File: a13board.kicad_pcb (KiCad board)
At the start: 4 copper layers, 50 x 90.4 mm, 152 parts, among them P1 CONN_20, P2 CONN_20, P3 CONN_20, P4 CONN_20, P5 CONN_20, U1 H27UBG8T2A/TSOP48, U2 A13, U3 H5TQ2G43CFR, U4 H5TQ2G43CFR, U5 OLIMEX_IC_AXP209, U6 SY8008BAAC, U7 SY8008BAAC, X1 CRYSTAL4

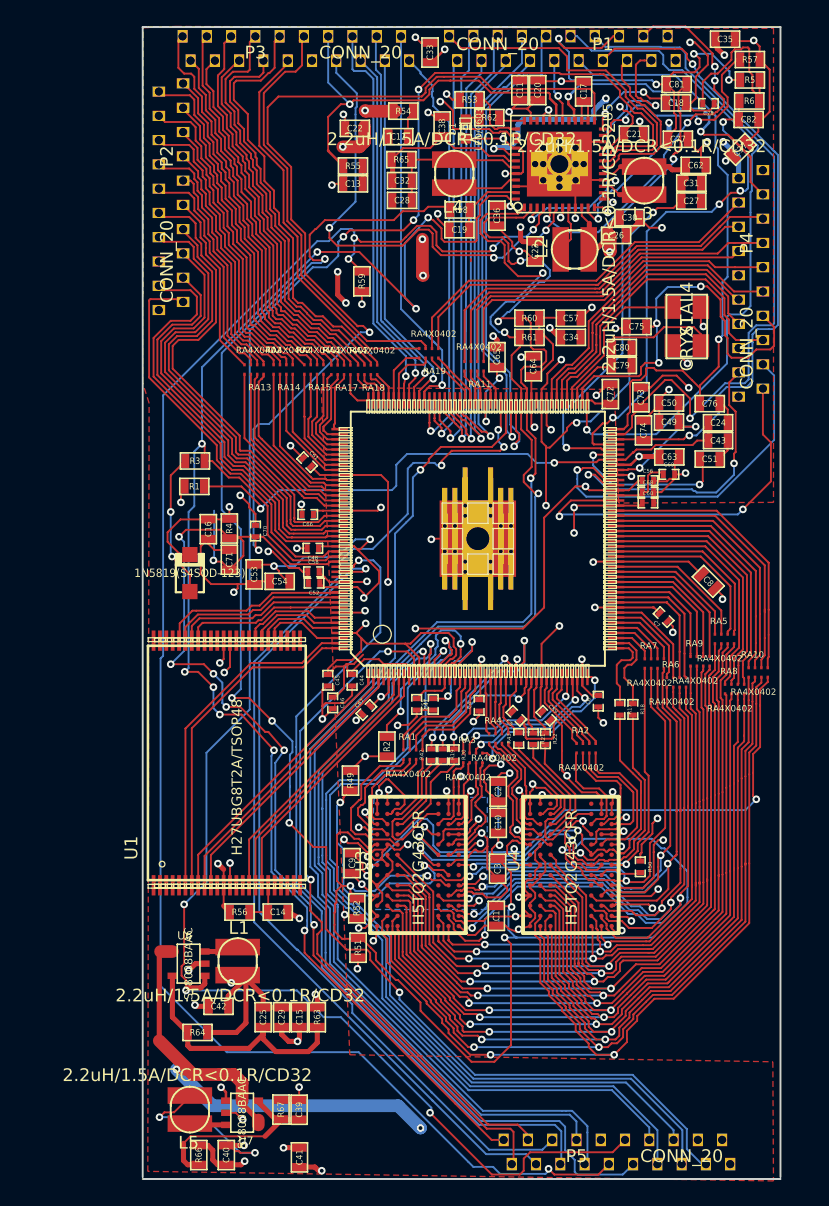
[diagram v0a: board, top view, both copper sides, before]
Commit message: Updated layout with people's suggestions
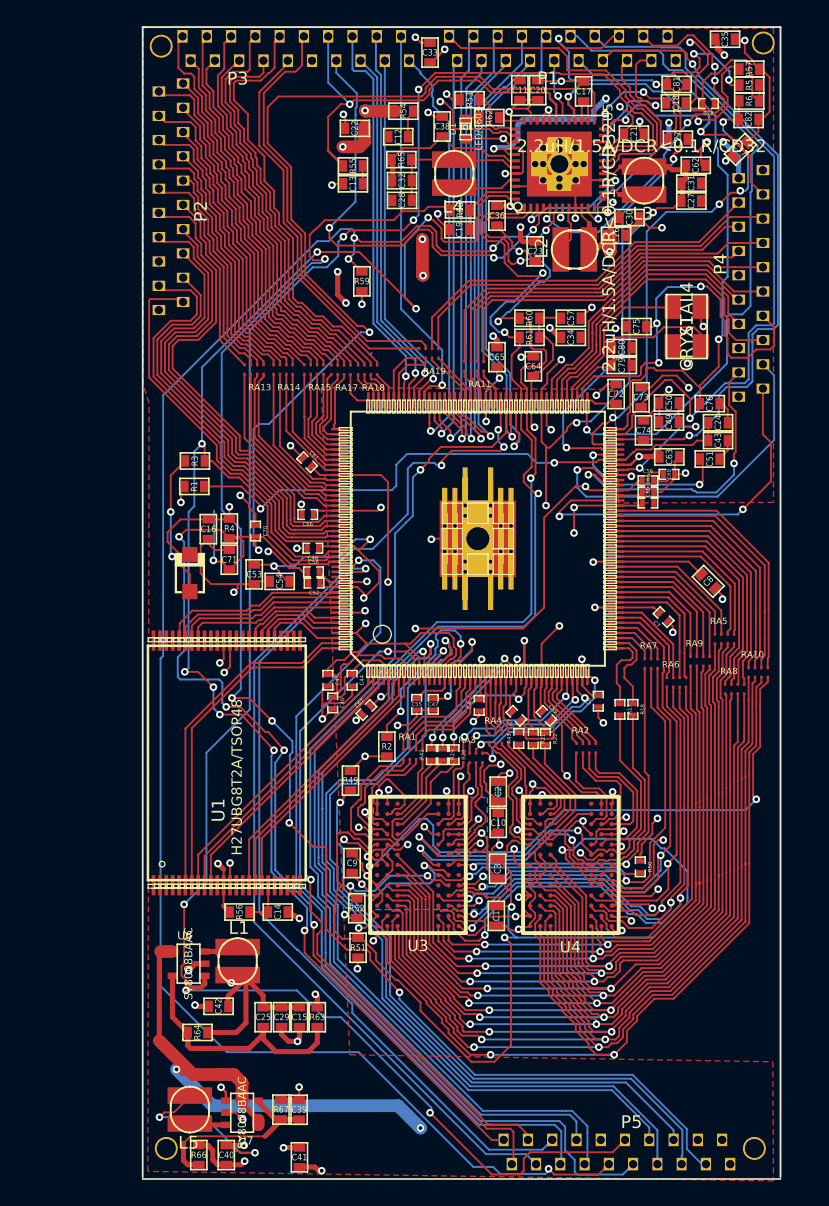
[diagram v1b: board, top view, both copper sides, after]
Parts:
- added P6: CONN_1, 1pin, F.Cu at (89.0, 138.8)
- added P7: CONN_1, 1pin, F.Cu at (135.9, 52.1)
- added P8: CONN_1, 1pin, F.Cu at (88.7, 52.4)
- added P9: CONN_1, 1pin, F.Cu at (135.2, 138.8)
- C10, C11, C12, C13, C14, C15, C16, C17, C18, C19, C20, C21, C22, C23, C24, C25, C26, C27, C28, C29, C30, C31, C32, C33, C34, C35, C36, C37, C38, C39, C40, C41, C42, C43, C49, C50, C51, C53, C54, C57, C62, C63, C64, C65, C71, C72, C73, C74, C75, C76, C77, C79, C8, C80, C81, C82, C9: footprint SM0603_Capa -> SM0603A
- R1, R2, R3, R4, R49, R5, R51, R52, R53, R54, R55, R56, R57, R58, R59, R6, R60, R61, R62, R63, R64, R65, R66, R67: footprint SM0603 -> SM0603A
- moved R57 0.75 mm to (134.8, 54.1)
- moved C72 0.45 mm to (124.3, 79.7)
- moved R5 0.40 mm to (134.8, 55.4)
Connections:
- U5 pad GND: GND -> (no net)
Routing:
- net +3.3V: track 184.0 -> 175.6 mm
- net /power/VDD_CPU: track 129.2 -> 133.8 mm
- net VPP: track 149.1 -> 147.0 mm
- net IPSOUT: track 229.5 -> 231.3 mm
- net N-00000277: track 12.8 -> 11.4 mm
- net RESET: track 162.5 -> 162.3 mm, vias 9 -> 7

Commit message: Used polygon for power pins
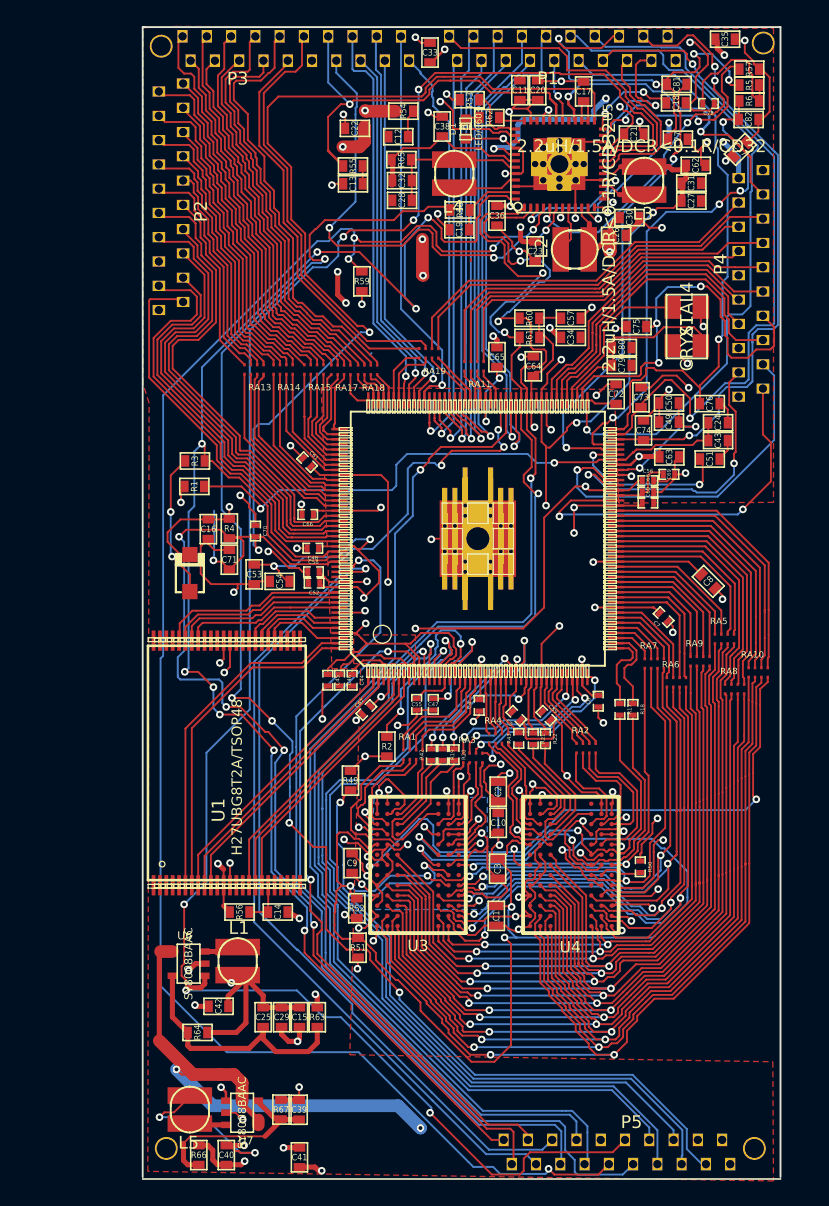
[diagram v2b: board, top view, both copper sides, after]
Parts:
- moved C46 1.87 mm to (102.7, 102.1)
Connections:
- U5 pad GND: (no net) -> GND
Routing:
- net /power/VDD_CPU: track 133.8 -> 126.1 mm
- net GND: track 265.1 -> 260.5 mm
- added copper zone on F.Cu, net /power/VDD_CPU

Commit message: Fixed some power issues
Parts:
- moved C40 9.03 mm to (102.0, 135.8)
- moved R66 8.53 mm to (99.3, 135.8)
- moved R63 8.15 mm to (92.8, 128.6)
- moved C41 5.45 mm to (103.5, 135.8)
- moved R64 2.68 mm to (93.9, 128.6), turned to 90 degrees
- moved C42 2.27 mm to (95.2, 128.6), turned to 90 degrees
- moved C39 1.18 mm to (100.7, 135.8)
- moved L5 0.18 mm to (90.8, 135.7)
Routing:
- net N-00000172: track 15.1 -> 5.19 mm
- net IPSOUT: track 231.3 -> 224.1 mm, vias 13 -> 14
- net N-00000171: track 20.2 -> 16.7 mm
- net +3.3V: track 175.6 -> 172.2 mm
- net VMEM: track 170.3 -> 172.9 mm, vias 30 -> 26
- net GND: track 260.5 -> 259.7 mm, vias 76 -> 74

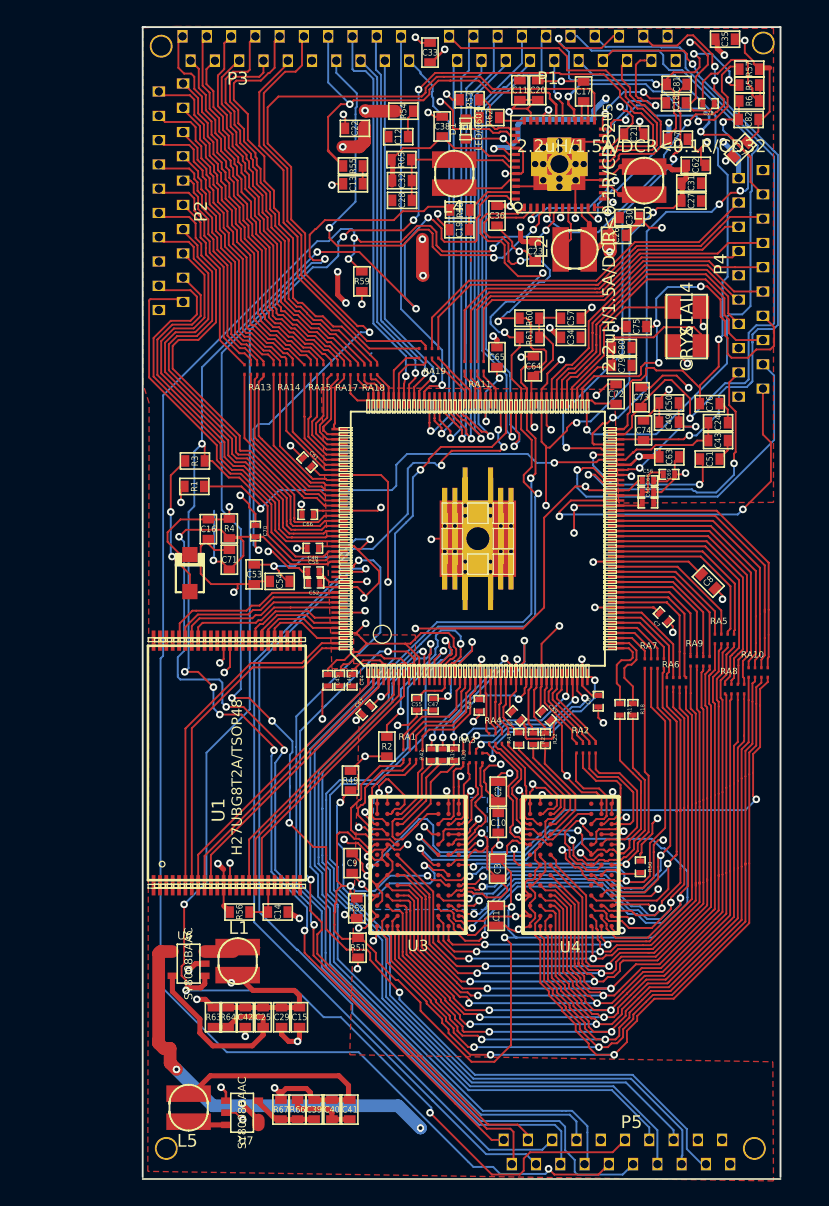
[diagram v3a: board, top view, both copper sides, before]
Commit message: A little fit of border clearance fixed
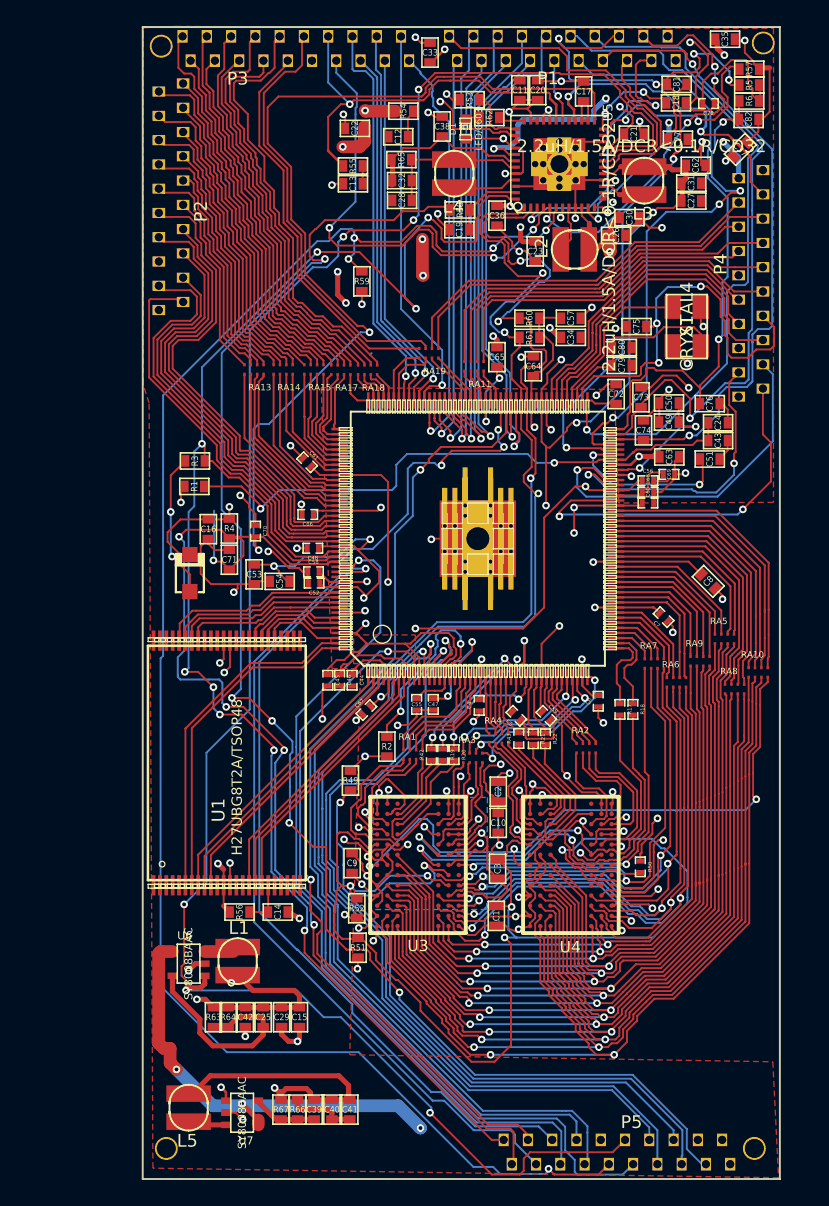
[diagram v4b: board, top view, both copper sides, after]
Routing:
- net TPX2: track 53.9 -> 52.5 mm
- net TPY2: track 49.1 -> 49.9 mm
- net LRADC: track 51.1 -> 50.4 mm
- net N-00000278: track 38.9 -> 39.6 mm
- net PB17: track 64.6 -> 64.0 mm
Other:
- outline, holes or cut-outs redrawn

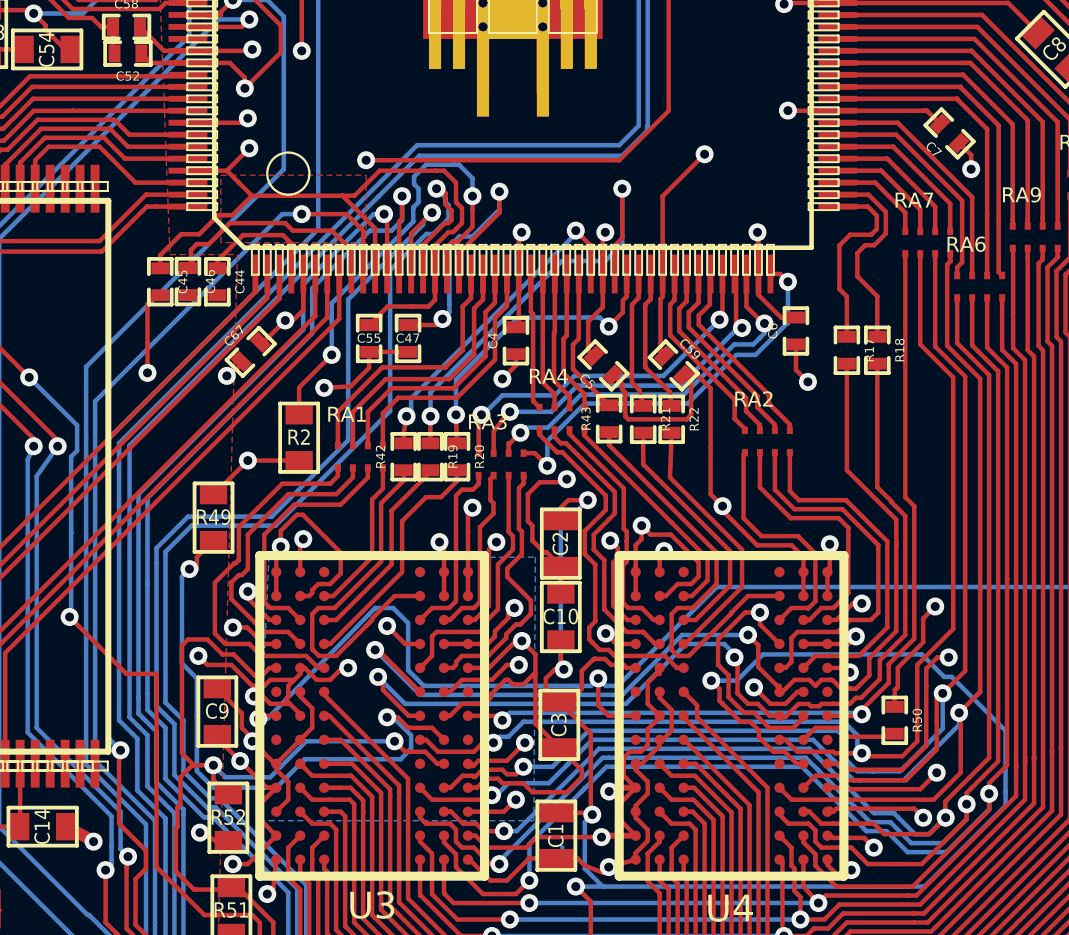
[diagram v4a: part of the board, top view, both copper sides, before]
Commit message: Improved data lines
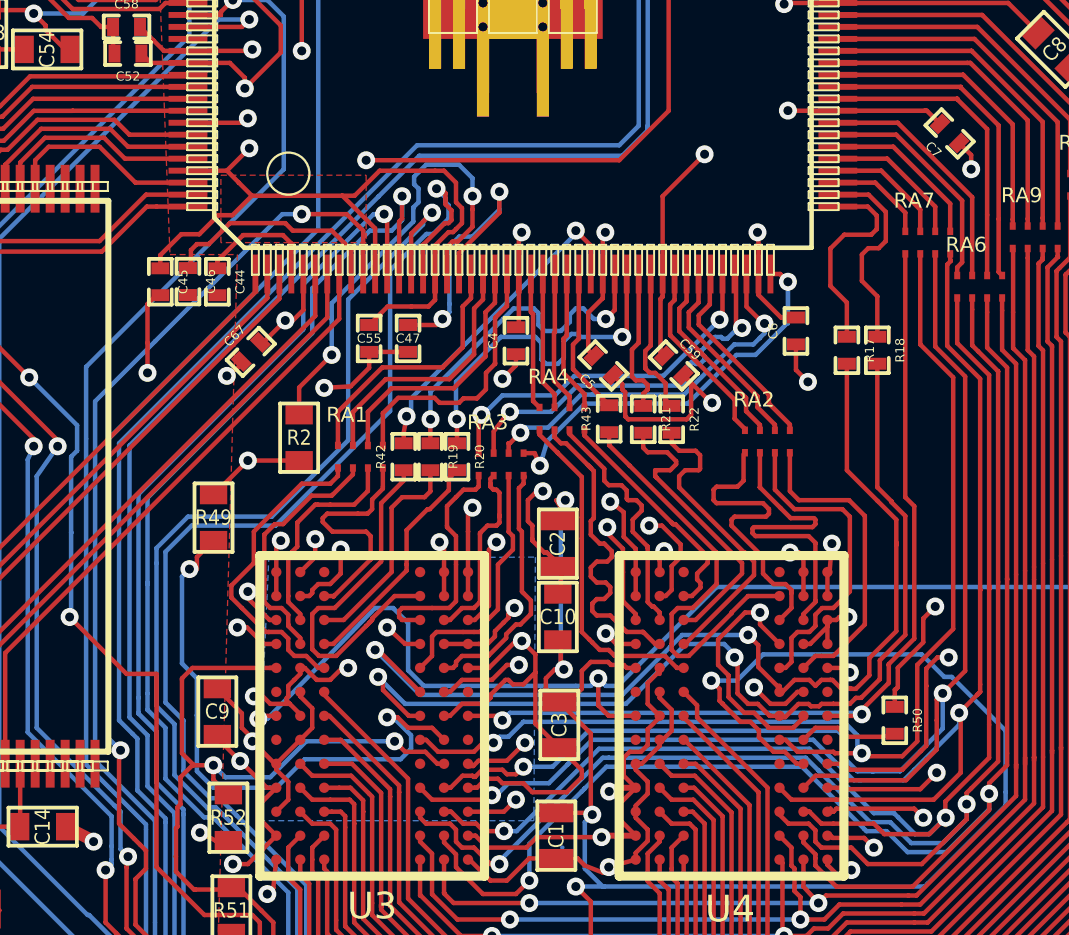
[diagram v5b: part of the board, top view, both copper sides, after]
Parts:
- moved C10 0.10 mm to (115.0, 113.3)
- moved C2 0.10 mm to (115.0, 110.8)
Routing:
- net GND: track 259.3 -> 248.0 mm, vias 74 -> 76
- net /DRAM/CPU_DQS0: track 15.1 -> 11.7 mm
- net /DRAM/DDR3_D0: track 5.26 -> 8.15 mm
- net N-0000056: track 106.4 -> 104.1 mm
- net /DRAM/DDR3_D12: track 8.11 -> 10.4 mm
- net /DRAM/DDR3_D8: track 8.72 -> 10.9 mm
- net /DRAM/DDR3_D1: track 6.19 -> 8.02 mm
- net /DRAM/DDR3_D4: track 12.3 -> 10.7 mm
- net /DRAM/CPU_DQS0_N: track 10.2 -> 11.9 mm
- net /DRAM/DDR3_D9: track 9.74 -> 11.4 mm
- net /DRAM/DDR3_D6: track 9.97 -> 8.37 mm
- net /DRAM/DDR3_DQS1: track 8.33 -> 9.91 mm
- net /DRAM/DDR3_D14: track 12.2 -> 10.7 mm
- net /DRAM/DDR3_DQS1_N: track 8.88 -> 10.4 mm
- net /DRAM/DDR3_D10: track 11.5 -> 10.4 mm
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
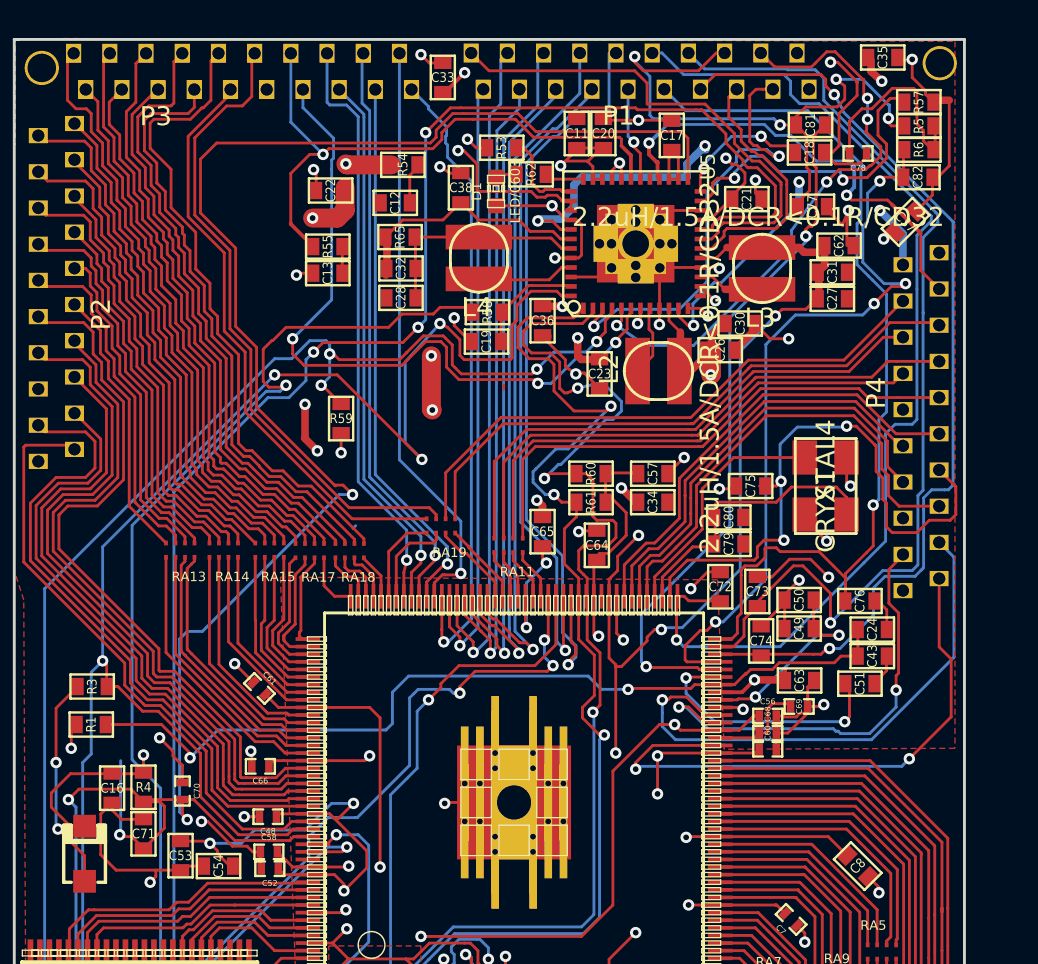
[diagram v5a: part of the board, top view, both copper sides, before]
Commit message: Fixed some symbols, hidden some silk
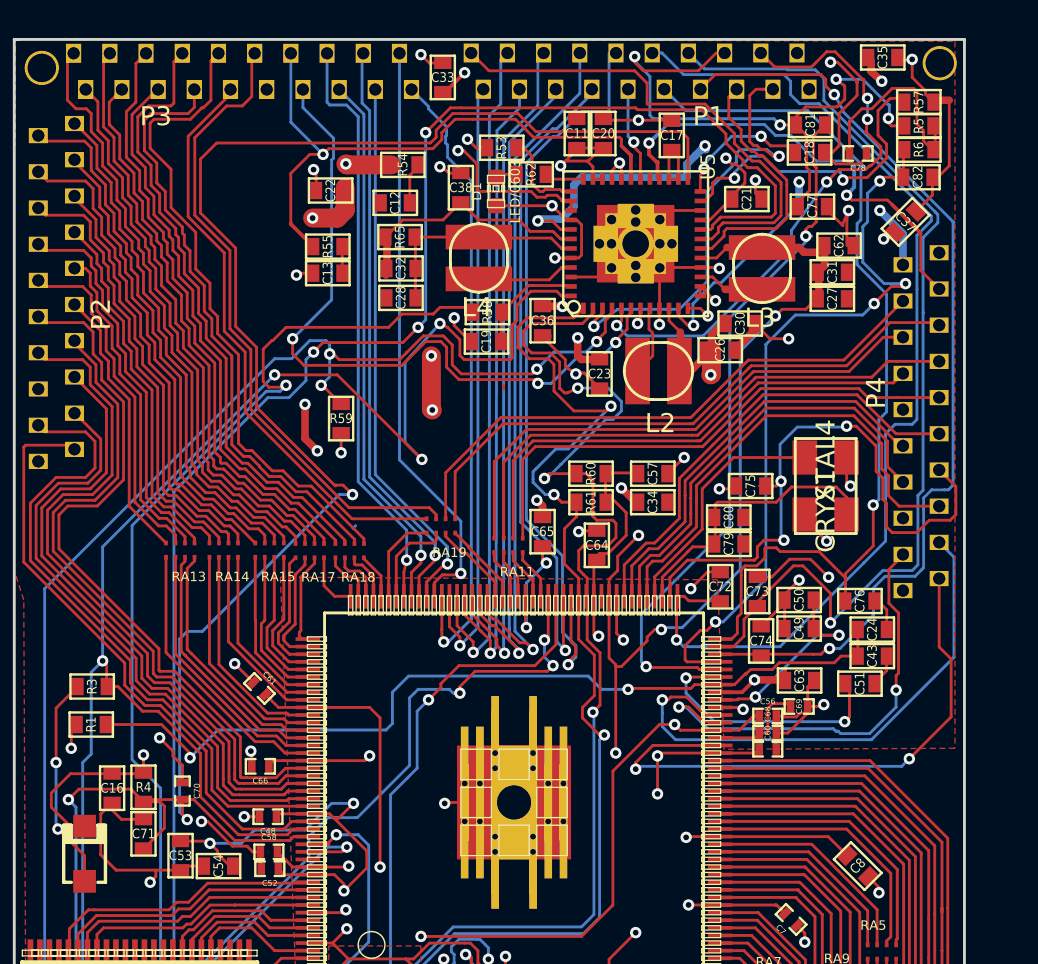
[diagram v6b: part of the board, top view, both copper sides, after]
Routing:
- net RESET: track 162.4 -> 156.8 mm, vias 7 -> 6
